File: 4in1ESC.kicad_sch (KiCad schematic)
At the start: 62 parts, among them U1 INA199A1DCKR, U14 HC-1_0-8PWT, U18 LMR51420YDDCR, U26 TPS746-3.3DRV, U5 XRIM160808SR47MBCD

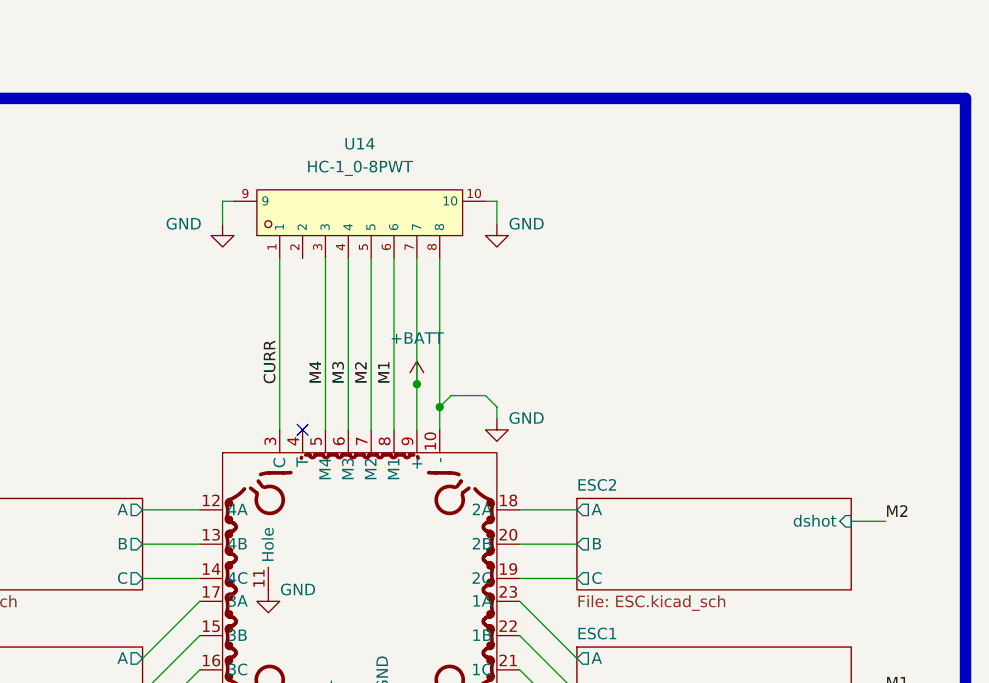
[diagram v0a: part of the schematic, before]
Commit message: Replaced the old ESC Connector with JST-SH series
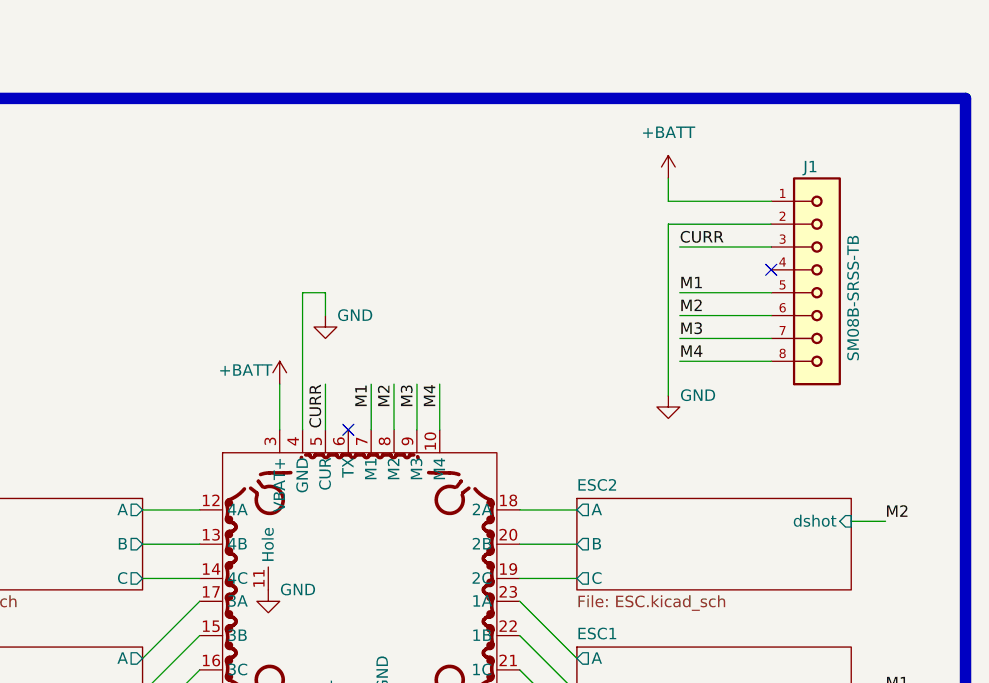
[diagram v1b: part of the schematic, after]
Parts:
- removed U14: HC-1_0-8PWT, components:CONN-SMD_HC-1.0-8PWT, symbol components:HC-1_0-8PWT
- added J1: SM08B-SRSS-TB, Connector_JST:JST_SH_SM08B-SRSS-TB_1x08-1MP_P1.00mm_Horizontal, symbol SM08B-SRSS-TB:SM08B-SRSS-TB
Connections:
- net +BATT: now also U4.3 (VBAT+), J1.1; no longer U4.9 (+)
- net CURR: now also U4.5 (CUR), J1.3; no longer U4.3 (C)
- net GND: now also U4.4 (GND), J1.2; no longer U4.10 (-)
- net M1: now also U4.7 (M1), J1.5; no longer U4.8 (M1)
- net M2: now also U4.8 (M2), J1.6; no longer U4.7 (M2)
- net M3: now also U4.9 (M3), J1.7; no longer U4.6 (M3)
- net M4: now also U4.10 (M4), J1.8; no longer U4.5 (M4)
- no-connect marks 1 -> 2
